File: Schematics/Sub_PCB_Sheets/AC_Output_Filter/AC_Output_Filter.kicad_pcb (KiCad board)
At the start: 2 copper layers, 494.6 x 179.4 mm, 277 parts, among them IC1 F280049CPMSR, IC2 CP2102N-A02-GQFN24R, IC3 TPD2EUSB30ADRTR, J1 23AH8786-Red, J10 464379202, J11 464369202, J12 464379202, J13 43045-1212, J14 43650-0418, J15 43650-0418, J16 464369202, J17 464379202, J18 43650-0418, J19 FTSH-105-01-LM-D-K, J2 23AH8785-Black, J20 43045-1212, J21 43650-0418, J22 43650-0418, J23 464369202, J24 43650-0418, J25 43650-0418, J26 43650-0418, J27 43650-0418, J28 1051330011, J3 23AH8786-Red, J4 23AH8785-Black, J5 464379202, J6 464369202, J7 43650-0418, J8 464379202, J9 464369202, Q1 STB10NK60ZT4, Q2 C3M0025065K, Q3 C3M0025065K, Q4 C3M0025065K, Q5 C3M0025065K, Q6 PC817X1CSP9F, Q7 PC817X1CSP9F, Q8 STB10NK60ZT4, U1 UCC21710QDWRQ1, U2 UCC21710QDWRQ1, U3 UCC21710QDWRQ1, U4 UCC21710QDWRQ1, U5 TR05S3V3, Y1 ABM8-20.000MHZ-B2-T

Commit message: adding AC Output Filter Fab files
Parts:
- removed C1: 1 uF, SiC_Inverter:R71PI410050H6K
- removed C10, C12, C14, C15, C16, C2, C3, C4, C6, C8: 22 uF, SiC_Inverter:ESH226M500AL4AA
- removed C11, C13, C5, C7, C9: 2 uF, SiC_Inverter:MKP1848C52050JK2
- removed C17, C18, C35, C36: 15 uF, Capacitor_SMD:C_1206_3216Metric_Pad1.33x1.80mm_HandSolder
- removed C19, C20, C26, C29, C30, C33, C37, C38, C44, C47, C48, C51, C54, C55, C56, C57, C58, C60, C61, C62, C63, C66, C67: 0.1 uF, Capacitor_SMD:C_0805_2012Metric_Pad1.18x1.45mm_HandSolder
- removed C21, C22, C27, C34, C39, C40, C45, C52, C69: 1 uF, Capacitor_SMD:C_1206_3216Metric_Pad1.33x1.80mm_HandSolder
- removed C23, C24, C25, C28, C31, C32, C41, C42, C43, C46, C49, C50: 100 pF, Capacitor_SMD:C_0603_1608Metric_Pad1.08x0.95mm_HandSolder
- removed C59, C68: 10 uF, Capacitor_SMD:C_0805_2012Metric_Pad1.18x1.45mm_HandSolder
- removed C64, C65: 18 pF, Capacitor_SMD:C_0402_1005Metric_Pad0.74x0.62mm_HandSolder
- removed D1, D7: BZX84C15-7-F, Package_TO_SOT_SMD:SOT-23-3
- removed D2, D3, D4, D5: BZX84C20-7-F, Package_TO_SOT_SMD:SOT-23-3
- removed D6: P6KE500A-HF, Diode_THT:D_DO-15_P12.70mm_Horizontal
- removed F1: 0031.8322, SiC_Inverter:0031.8322
- removed the G*** at (67.5, 176.0)
- removed the G*** at (153.3, 177.6)
- removed the G*** at (299.4, 164.9)
- removed the G*** at (224.0, 180.9)
- removed the G*** at (382.6, 134.4)
- removed the G*** at (299.1, 62.0)
- removed the G*** at (142.9, 100.9)
- removed H1, H10, H11, H12, H13, H14, H15, H16, H17, H18, H19, H2, H20, H21, H22, H23, H24, H25, H26, H27, H28, H3, H4, H5, H6, H7, H8, H9: MountingHole, MountingHole:MountingHole_2.2mm_M2
- removed IC1: F280049CPMSR, SiC_Inverter:F280049CPMSR
- removed IC2: CP2102N-A02-GQFN24R, SiC_Inverter:CP2102N-A02-GQFN24R
- removed IC3: TPD2EUSB30ADRTR, SiC_Inverter:TPD2EUSB30ADRTR
- removed J1: 23AH8786-Red, SiC_Inverter:23AH8786-Red
- removed J10, J12, J5, J8: 464379202, SiC_Inverter:46437-900_02
- removed J11, J16, J23, J6, J9: 464369202, SiC_Inverter:46436-900_02
- removed J13, J20: 43045-1212, SiC_Inverter:43045-1212
- removed J14, J15, J18, J21, J22, J24, J25, J26, J27, J7: 43650-0418, SiC_Inverter:436500418
- removed J19: FTSH-105-01-LM-D-K, SiC_Inverter:FTSH-105-01-LM-D-K
- removed J2: 23AH8785-Black, SiC_Inverter:23AH8785-Black
- removed J28: 1051330011, SiC_Inverter:105133-0011
- removed L1: 47 uH, SiC_Inverter:2300HT_470
- removed L2: 2.2 mH, SiC_Inverter:7448258022
- removed PS1, PS2: IRM-03-15, SiC_Inverter:IRM-03-15
- removed Q1, Q8: STB10NK60ZT4, Package_TO_SOT_SMD:TO-263-2
- removed Q2, Q3, Q4, Q5: C3M0025065K, SiC_Inverter:C3M0025065K
- removed Q6, Q7: PC817X1CSP9F, SiC_Inverter:PC817X1CSP9F
- removed R1, R44, R45: 499 K, Resistor_SMD:R_1206_3216Metric_Pad1.30x1.75mm_HandSolder
- removed R10, R21, R22, R23, R24, R7, R8, R9: 10, Resistor_SMD:R_1206_3216Metric_Pad1.30x1.75mm_HandSolder
- removed R11, R13, R14, R16, R17, R18, R25, R27, R28, R30, R31, R32: 5 K, Resistor_SMD:R_1206_3216Metric_Pad1.30x1.75mm_HandSolder
- removed R12, R15, R26, R29: 100, Resistor_SMD:R_1206_3216Metric_Pad1.30x1.75mm_HandSolder
- removed R19, R20, R34, R36, R37, R39, R4, R40, R41, R43, R47, R48, R5, R6: 100 K, Resistor_SMD:R_1206_3216Metric_Pad1.30x1.75mm_HandSolder
- removed R2: CW005100R0JE12HE, SiC_Inverter:CW005100R0JE12HE
- removed R3, R46: 47, Resistor_SMD:R_1206_3216Metric_Pad1.30x1.75mm_HandSolder
- removed R35, R42: 10 K, Resistor_SMD:R_1206_3216Metric_Pad1.30x1.75mm_HandSolder
- removed R38: 2 K, Resistor_SMD:R_1206_3216Metric_Pad1.30x1.75mm_HandSolder
- removed R49: 0, Resistor_SMD:R_1206_3216Metric_Pad1.30x1.75mm_HandSolder
- removed TP1, TP11, TP24, TP25, TP26, TP27, TP32, TP34, TP35, TP36, TP37, TP38, TP40, TP41, TP42, TP43, TP44, TP45, TP46, TP47, TP48, TP49, TP5, TP50, TP51, TP52, TP53, TP54, TP55, TP56, TP57, TP58, TP60, TP61, TP62, TP63, TP64, TP65, TP67, TP69, TP7, TP71, TP72, TP74, TP8: 5277, SiC_Inverter:5277
- removed TP10, TP2, TP33, TP39, TP59, TP6, TP66, TP68, TP70, TP73, TP75, TP76, TP9: 5281, SiC_Inverter:5281
- removed U1, U2, U3, U4: UCC21710QDWRQ1, SiC_Inverter:UCC21710QDWRQ1
- removed U5: TR05S3V3, SiC_Inverter:TR05S3V3
- removed Y1: ABM8-20.000MHZ-B2-T, SiC_Inverter:ABM8-20.000MHZ-B2-T
- J3: value 23AH8786-Red -> CONN_66.9040-21_MTC
- J4: value 23AH8785-Black -> CONN_66.9040-21_MTC
- moved TP4 342.1 mm to (168.8, 94.8)
- moved C53 341.9 mm to (177.9, 45.6)
- moved G*** 341.9 mm to (173.1, 62.1)
- moved H29 341.9 mm to (191.0, 24.6)
- moved H31 341.9 mm to (108.7, 24.6)
- moved R33 341.9 mm to (166.4, 48.2)
- moved H30 341.9 mm to (190.9, 104.8)
- moved H32 341.9 mm to (108.8, 104.8)
- moved J4 341.9 mm to (183.1, 94.8)
- moved L4 341.9 mm to (125.5, 87.7)
- moved J17 341.7 mm to (107.9, 60.9)
- moved L3 341.7 mm to (125.5, 42.5)
- moved J3 341.2 mm to (183.1, 34.5)
- moved TP3 339.9 mm to (168.8, 34.5)
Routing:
- net LOGIC_GND: track 232.6 -> 0.00 mm, vias 36 -> 0
- net +3V3: track 194.4 -> 0.00 mm, vias 32 -> 0
- net GND: track 192.5 -> 0.00 mm, vias 24 -> 0
- net /Con_Pro_Gate_node_output: track 154.7 -> 0.00 mm, vias 1 -> 0
- net +15V_ISO_LALS: track 150.9 -> 0.00 mm
- net GND_ISO_LAHS: track 137.6 -> 0.00 mm, vias 6 -> 0
- net /Con_PWM_A_H: track 116.7 -> 0.00 mm, vias 1 -> 0
- net /Con_PWM_A_L: track 104.9 -> 0.00 mm, vias 1 -> 0
- net /Con_EN_B_H: track 104.7 -> 0.00 mm, vias 1 -> 0
- net /Con_PWM_B_H: track 97.3 -> 0.00 mm, vias 1 -> 0
- net /Con_PWM_B_L: track 92.3 -> 0.00 mm, vias 1 -> 0
- net /Con_EN_A_L: track 91.9 -> 0.00 mm, vias 1 -> 0
- net /Con_FLT_B_H: track 88.3 -> 0.00 mm, vias 1 -> 0
- net GND_ISO_LBHS: track 88.2 -> 0.00 mm, vias 10 -> 0
- net /Con_RDY_A_H: track 85.5 -> 0.00 mm, vias 1 -> 0
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- removed copper zone on B.Cu, net +3V3
- removed copper zone on F.Cu, net +VIN
- removed copper zone on F.Cu, net -VIN
- removed copper zone on F.Cu, net /DC_Link_Caps/BUS_DC+
- removed copper zone on F.Cu, net /EMI_Input_Filter/+VIN_EMI
- removed copper zone on F.Cu, net /EMI_Input_Filter/BUS+_Filtered
- removed copper zone on F.Cu, net /EMI_Input_Filter/BUS+_RAW
- removed copper zone on B.Cu, net GND
- removed copper zone on B.Cu, net LOGIC_GND
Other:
- board size 494.6 x 179.4 mm -> 93 x 90.5 mm
- board text removed: "(325-425) VDC Input"
- board text removed: "+15VDC"
- board text removed: "+3V3"
- board text removed: "+DC Filtered"
- board text removed: "+DC_BUS"
- board text removed: "+VIN"
- board text removed: "+VIN_Pro"
- board text removed: "-VIN"
- board text removed: "2.08 Inches"
- board text removed: "CPro G_Node"
- board text removed: "Controller + USB"
- board text removed: "DC Input / Protection Circuit"
- board text removed: "DC Input and Input Protection Circuit"
- board text removed: "DC Link Caps"
- board text removed: "DC+"
- board text removed: "EMI Input Filter"
- board text removed: "EN_AH"
- board text removed: "EN_AL"
- board text removed: "EN_BH"
- board text removed: "EN_BL"
- board text removed: "FLT_AH"
- board text removed: "FLT_AL"
- board text removed: "FLT_BH"
- board text removed: "FLT_BL"
- board text removed: "Full-Bridge"
- board text removed: "GND"
- board text removed: "G_Node"
- board text removed: "HS_Gate"
- board text removed: "High Side"
- board text removed: "High to Low Voltage Board"
- board text removed: "ISO_GND"
- board text removed: "J-TAG"
- board text removed: "LAHS"
- board text removed: "LALS"
- board text removed: "LBHS"
- board text removed: "LBLS"
- board text removed: "LS_Gate"
- board text removed: "L_GND"
- board text removed: "Leg A"
- board text removed: "Leg B"
- board text removed: "Logic GND"
- board text removed: "Low Side"
- board text removed: "Need to move to a 4 layer board when on its own PCB sheet"
- board text removed: "Open Loop Design"
- board text removed: "PWM AH"
- board text removed: "PWM AL"
- board text removed: "PWM BH"
- board text removed: "PWM BL"
- board text removed: "PWM_A_H"
- board text removed: "PWM_A_L"
- board text removed: "PWM_B_H"
- board text removed: "PWM_B_L"
- board text removed: "Phase A Node"
- board text removed: "Phase B Node"
- board text removed: "Power"
- board text removed: "Pre G_Node"
- board text removed: "Pre-Charge Circuit"
- board text removed: "Pre-Charge_Current_Limiting"
- board text removed: "Pro G_Node"
- board text removed: "RDY_AH"
- board text removed: "RDY_AL"
- board text removed: "RDY_BH"
- board text removed: "RDY_BL"
- board text removed: "SiC Full Bridge"
- board text removed: "SiC Single Phase Inverter Controller"
- board text removed: "TCK"
- board text removed: "TDI"
- board text removed: "TDO"
- board text removed: "TMS"
- board text removed: "To Controller J18"
- board text removed: "To Controller J20"
- board text removed: "To Controller J21"
- board text removed: "To Controller J22"
- board text removed: "To DC Input J24"
- board text removed: "To Full-Bridge J13"
- board text removed: "To Full-Bridge J14"
- board text removed: "To Full-Bridge J15"
- board text removed: "To Power Board J25"
- board text removed: "To Power J26"
- board text removed: "To Power J27"
- board text removed: "To Pre-Charge J7"
- board text removed: "X1"
- board text removed: "X2"
- board text removed: "XRS"

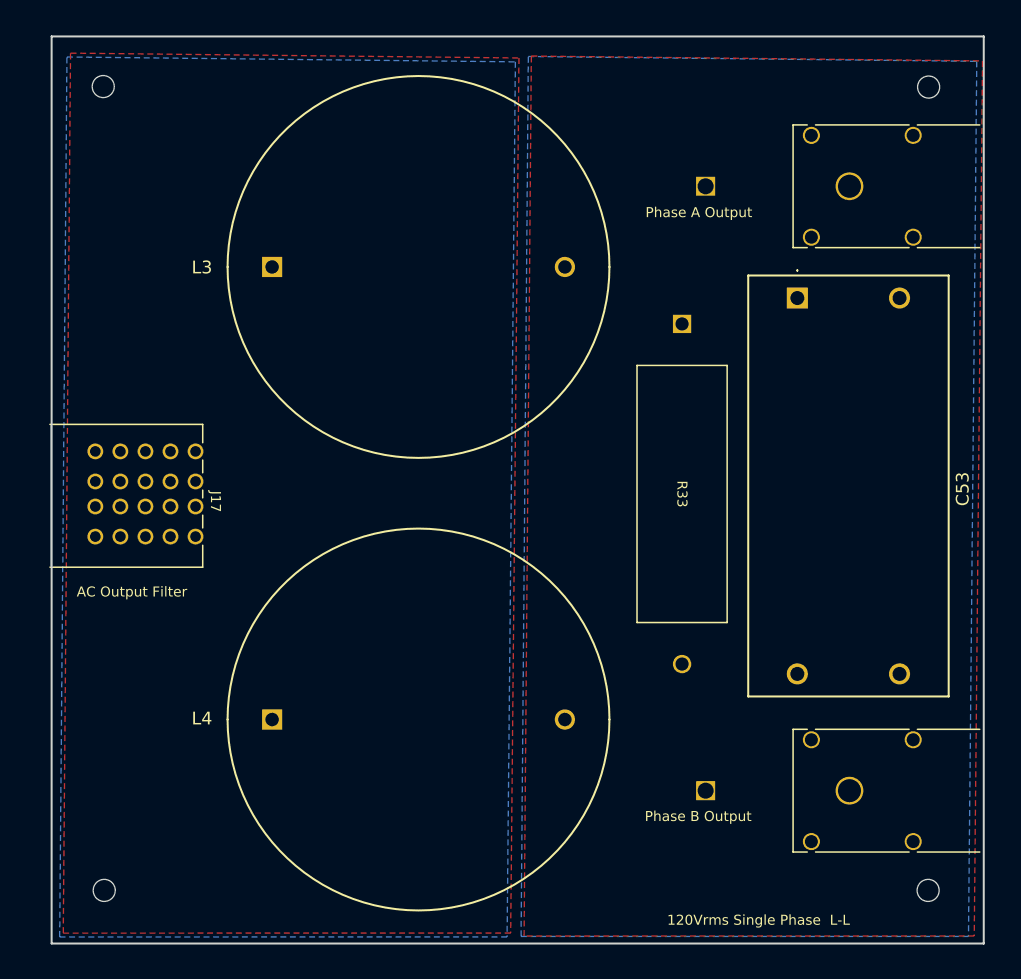
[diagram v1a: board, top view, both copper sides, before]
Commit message: Cleaning up power planes before Fab Output
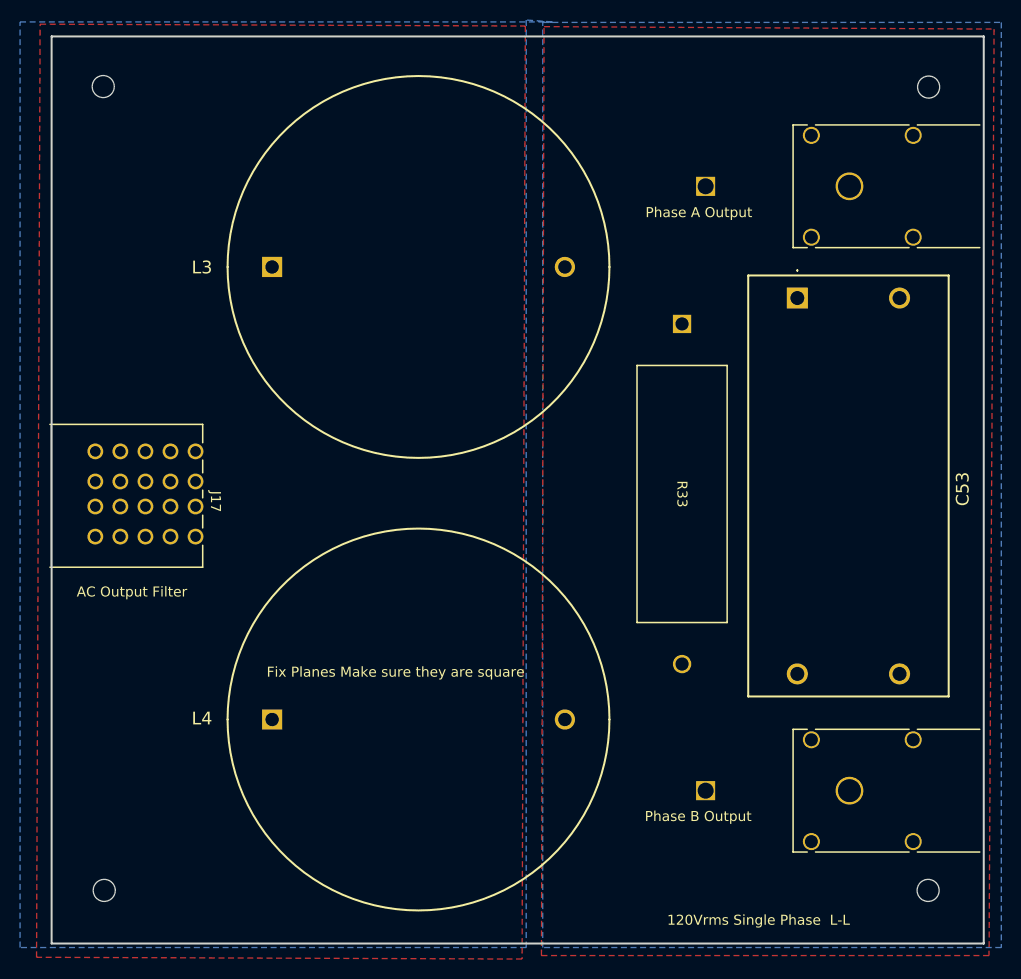
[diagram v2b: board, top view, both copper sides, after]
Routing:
- added copper zone on F.Cu, net GND_ISO_LAHS
- added copper zone on B.Cu, net GND_ISO_LBHS
- removed copper zone on B.Cu, net GND_ISO_LAHS
- removed copper zone on F.Cu, net GND_ISO_LBHS
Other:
- board text added: "Fix Planes Make sure they are square"
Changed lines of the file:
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@@
+		)
+	)
+	(gr_text "Fix Planes Make sure they are square"
+		(at 124.95 83.55 0)
+		(layer "F.SilkS")
+		(effects
+			(font
+				(size 1 1)
+				(thickness 0.15)
+			)
+			(justify left bottom)
 		)
 	)
@@
 				(margins 1.0025 1.0025 1.0025 1.0025)
 				(span 4 1)
-				(layer "F.Cu")
+				(layer "Cmts.User")
 				(effects
 					(font
@@
 				(margins 1.0025 1.0025 1.0025 1.0025)
 				(span 0 1)
-				(layer "F.Cu")
+				(layer "Cmts.User")
 				(effects
 					(font
@@
 				(margins 1.0025 1.0025 1.0025 1.0025)
 				(span 0 1)
-				(layer "F.Cu")
+				(layer "Cmts.User")
 				(effects
 					(font
@@
 				(margins 1.0025 1.0025 1.0025 1.0025)
 				(span 0 1)
-				(layer "F.Cu")
+				(layer "Cmts.User")
 				(effects
 					(font
@@
 				(margins 1.0025 1.0025 1.0025 1.0025)
 				(span 1 1)
-				(layer "F.Cu")
+				(layer "Cmts.User")
 				(effects
 					(font
@@
 				(margins 1.0025 1.0025 1.0025 1.0025)
 				(span 1 1)
-				(layer "F.Cu")
+				(layer "Cmts.User")
 				(effects
 					(font
@@
 				(margins 1.0025 1.0025 1.0025 1.0025)
 				(span 1 1)
-				(layer "F.Cu")
+				(layer "Cmts.User")
 				(effects
 					(font
@@
 				(margins 1.0025 1.0025 1.0025 1.0025)
 				(span 1 1)
-				(layer "F.Cu")
+				(layer "Cmts.User")
 				(effects
 					(font
@@
 				(margins 1.0025 1.0025 1.0025 1.0025)
 				(span 1 1)
-				(layer "F.Cu")
+				(layer "Cmts.User")
 				(effects
 					(font
@@
 				(margins 1.0025 1.0025 1.0025 1.0025)
 				(span 1 1)
-				(layer "F.Cu")
+				(layer "Cmts.User")
 				(effects
 					(font
@@
 				(margins 1.0025 1.0025 1.0025 1.0025)
 				(span 1 1)
-				(layer "F.Cu")
+				(layer "Cmts.User")
 				(effects
 					(font
@@
 				(margins 1.0025 1.0025 1.0025 1.0025)
 				(span 1 1)
-				(layer "F.Cu")
+				(layer "Cmts.User")
 				(effects
 					(font
@@
 				(margins 1.0025 1.0025 1.0025 1.0025)
 				(span 1 1)
-				(layer "F.Cu")
+				(layer "Cmts.User")
 				(effects
 					(font
@@
 				(margins 1.0025 1.0025 1.0025 1.0025)
 				(span 1 1)
-				(layer "F.Cu")
+				(layer "Cmts.User")
 				(effects
 					(font
@@
 				(margins 1.0025 1.0025 1.0025 1.0025)
 				(span 1 1)
-				(layer "F.Cu")
+				(layer "Cmts.User")
 				(effects
 					(font
@@
 				(margins 1.0025 1.0025 1.0025 1.0025)
 				(span 1 1)
-				(layer "F.Cu")
+				(layer "Cmts.User")
 				(effects
 					(font
@@
 				(margins 1.0025 1.0025 1.0025 1.0025)
 				(span 1 1)
-				(layer "F.Cu")
+				(layer "Cmts.User")
 				(effects
 					(font
@@
 				(margins 1.0025 1.0025 1.0025 1.0025)
 				(span 1 1)
-				(layer "F.Cu")
+				(layer "Cmts.User")
 				(effects
 					(font
@@
 				(margins 1.0025 1.0025 1.0025 1.0025)
 				(span 1 1)
-				(layer "F.Cu")
+				(layer "Cmts.User")
 				(effects
 					(font
@@
 				(margins 1.0025 1.0025 1.0025 1.0025)
 				(span 1 1)
-				(layer "F.Cu")
+				(layer "Cmts.User")
 				(effects
 					(font
@@
 				(margins 1.0025 1.0025 1.0025 1.0025)
 				(span 1 1)
-				(layer "F.Cu")
+				(layer "Cmts.User")
 				(effects
 					(font
@@
 				(margins 1.0025 1.0025 1.0025 1.0025)
 				(span 1 1)
-				(layer "F.Cu")
+				(layer "Cmts.User")
 				(effects
 					(font
@@
 				(margins 1.0025 1.0025 1.0025 1.0025)
 				(span 1 1)
-				(layer "F.Cu")
+				(layer "Cmts.User")
 				(effects
 					(font
@@
 				(margins 1.0025 1.0025 1.0025 1.0025)
 				(span 1 1)
-				(layer "F.Cu")
+				(layer "Cmts.User")
 				(effects
 					(font
@@
 				(margins 1.0025 1.0025 1.0025 1.0025)
 				(span 1 1)
-				(layer "F.Cu")
+				(layer "Cmts.User")
 				(effects
 					(font
@@
 				(margins 1.0025 1.0025 1.0025 1.0025)
 				(span 1 1)
-				(layer "F.Cu")
+				(layer "Cmts.User")
 				(effects
 					(font
@@
 				(margins 1.0025 1.0025 1.0025 1.0025)
 				(span 1 1)
-				(layer "F.Cu")
+				(layer "Cmts.User")
 				(effects
 					(font
@@
 				(margins 1.0025 1.0025 1.0025 1.0025)
 				(span 1 1)
-				(layer "F.Cu")
+				(layer "Cmts.User")
 				(effects
 					(font
@@
 	)
 	(zone
-		(net "GND_ISO_LBHS")
+		(net "GND_ISO_LAHS")
+		(locked yes)
 		(layer "F.Cu")
 		(name "Phase")
@@
 		(priority 12)
 		(connect_pads
-			(clearance 1)
+			(clearance 2)
 		)
 		(min_thickness 0.25)
@@
 		(polygon
 			(pts
-				(xy 105.386343 21.215667) (xy 150.12778 21.699885) (xy 149.300478 109.007163) (xy 104.662579 109.010502)
+				(xy 102.352722 18.325512) (xy 150.762381 18.510799) (xy 150.437584 111.599065) (xy 101.996394 111.422603)
 			)
 		)
@@
 		(priority 12)
 		(connect_pads
-			(clearance 1)
+			(clearance 2)
 		)
 		(min_thickness 0.25)
@@
 		(polygon
 			(pts
-				(xy 151.361859 21.505539) (xy 196.377302 21.992722) (xy 195.55 109.3) (xy 150.638071 109.303359)
+				(xy 152.628737 18.572178) (xy 197.531036 18.816841) (xy 197.027398 111.248257) (xy 152.3712 111.251597)
 			)
 		)
 	)
 	(zone
-		(net "GND_ISO_LAHS")
+		(net "/Phase_B_Output")
 		(layer "B.Cu")
-		(name "Phase")
 		(hatch edge 0.5)
-		(priority 12)
 		(connect_pads
-			(clearance 1)
+			(clearance 2)
 		)
 		(min_thickness 0.25)
@@
 		(polygon
 			(pts
-				(xy 105.0288 21.600337) (xy 149.770237 22.084555) (xy 148.942935 109.391833) (xy 104.305036 109.395172)
+				(xy 198.25 18.15) (xy 198.25 110.45) (xy 152.5 110.45) (xy 152.5 18.15)
 			)
 		)
 	)
 	(zone
-		(net "/Phase_B_Output")
+		(net "GND_ISO_LBHS")
 		(layer "B.Cu")
-		(name "Phase")
 		(hatch edge 0.5)
-		(priority 12)
+		(priority 1)
 		(connect_pads
-			(clearance 1)
+			(clearance 2)
 		)
 		(min_thickness 0.25)
@@
 		(polygon
 			(pts
-				(xy 151.061909 21.549373) (xy 195.803346 22.033591) (xy 194.976044 109.340869) (xy 150.338145 109.344208)
-			)
-		)
+				(xy 153.45 18.1) (xy 150.85 17.914286) (xy 150.85 110.45) (xy 100.35 110.45) (xy 100.35 18.1)
+			)
+		)
